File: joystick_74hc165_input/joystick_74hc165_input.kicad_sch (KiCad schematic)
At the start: 17 parts, among them J1 Conn_01x18, J2 Conn_02x14_Odd_Even

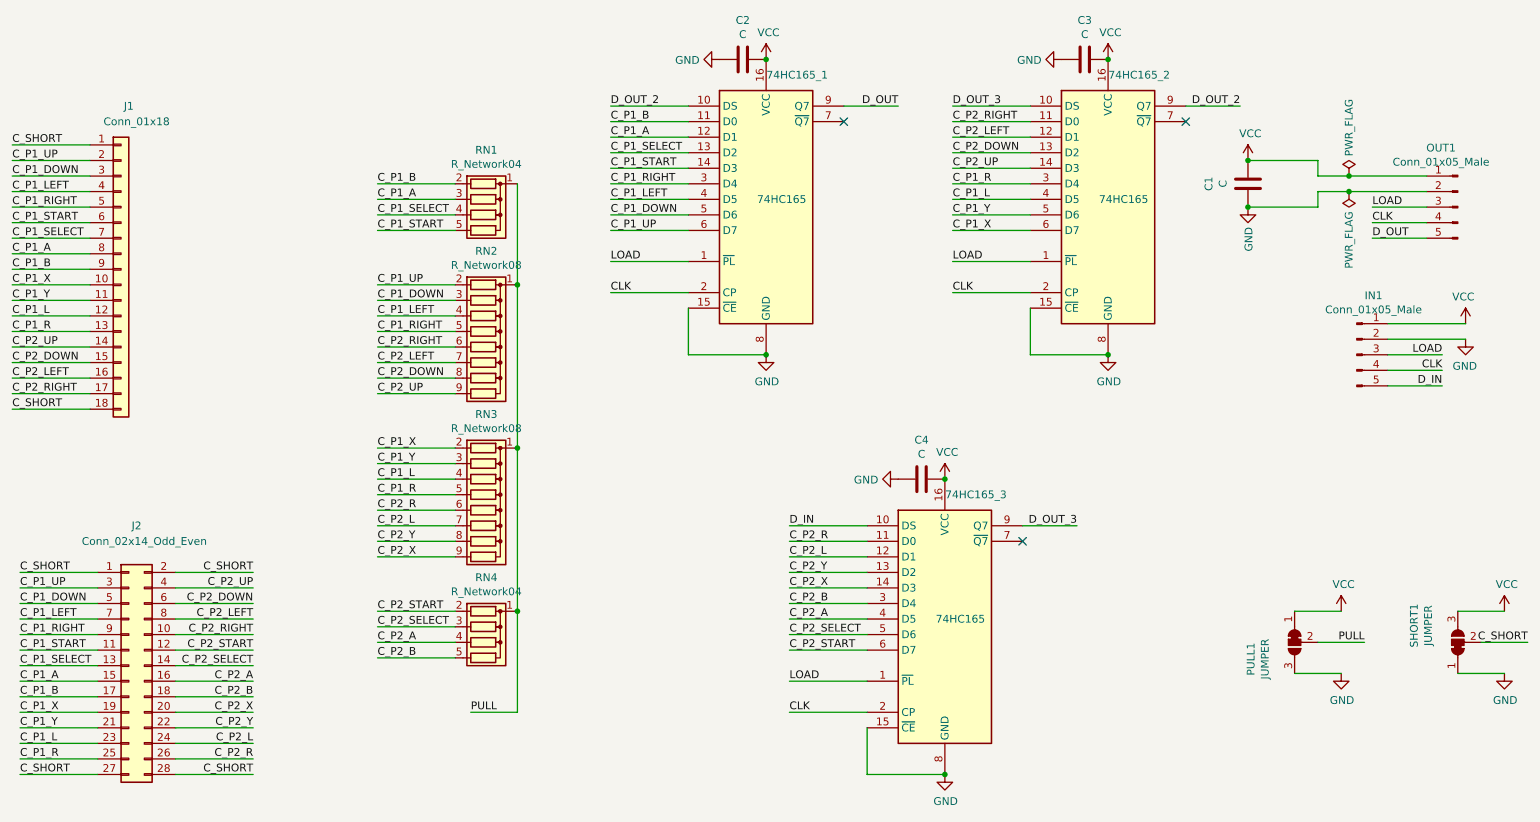
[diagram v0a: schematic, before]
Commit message: 부품 값 입력
Signed-off-by: Ju, Gyeong-min <jcmh74@gmail.com>
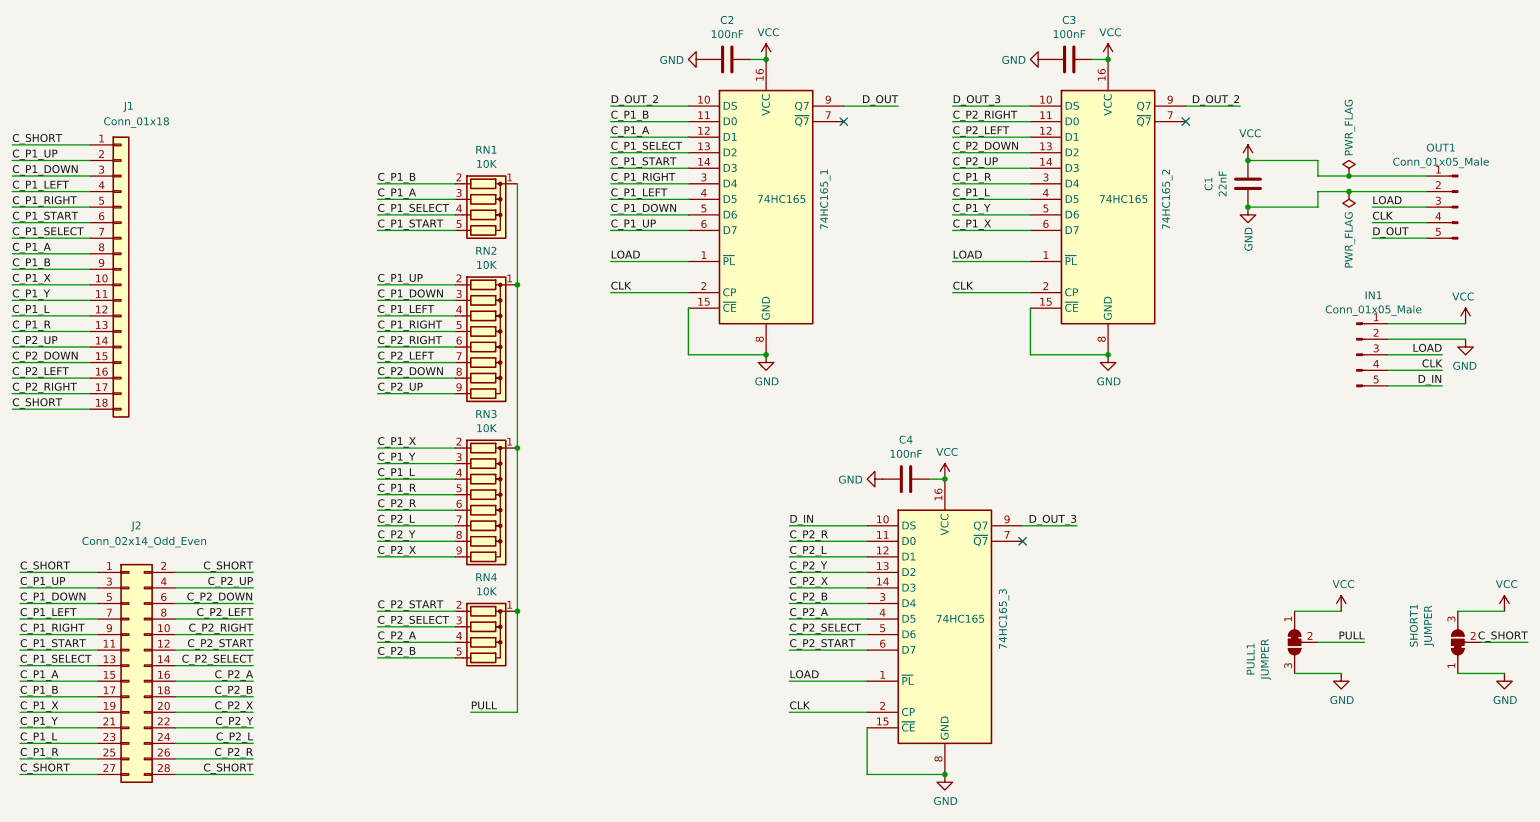
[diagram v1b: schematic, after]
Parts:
- C1: value C -> 22nF
- C2, C3, C4: value C -> 100nF
- RN1, RN4: value R_Network04 -> 10K
- RN2, RN3: value R_Network08 -> 10K
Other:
- moved on the sheet: C2, C3, C4
